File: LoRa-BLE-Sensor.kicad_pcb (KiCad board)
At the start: 4 copper layers, 96 x 60 mm, 129 parts, among them J1 SHF-105-01-X-D-SM, J10 Battery_with_NTC, J11 Conn_01x02_Socket, J12 Conn_01x02_Socket, J2 Conn_01x02_Socket, J3 Battery_with_NTC, J4 Conn_01x06_Socket, J5 Screw_Terminal_01x06, J6 Screw_Terminal_01x06, J7 Screw_Terminal_01x04, J8 Conn_01x04_Pin, J9 Conn_01x04_Pin, Q1 DMN67D7L, Q10 SQ2389ES, Q11 SQ2389ES, Q12 DMN62D0UDW-7, Q13 DMN62D0UDW-7, Q2 DMN67D7L, Q3 DMN67D7L, Q4 DMN67D7L, Q5 DMN67D7L, Q6 DMN67D7L, Q7 DMN67D7L, Q8 DMN67D7L, Q9 SQ2389ES, SW1 SW_Push, SW2 SW_Push, SW3 SW_Push, U1 RAK4630, U2 NPM1300-QEAA-R, U3 TLV61046ADBVR, U4 TLV61046ADBVR, U5 TLV61046ADBVR

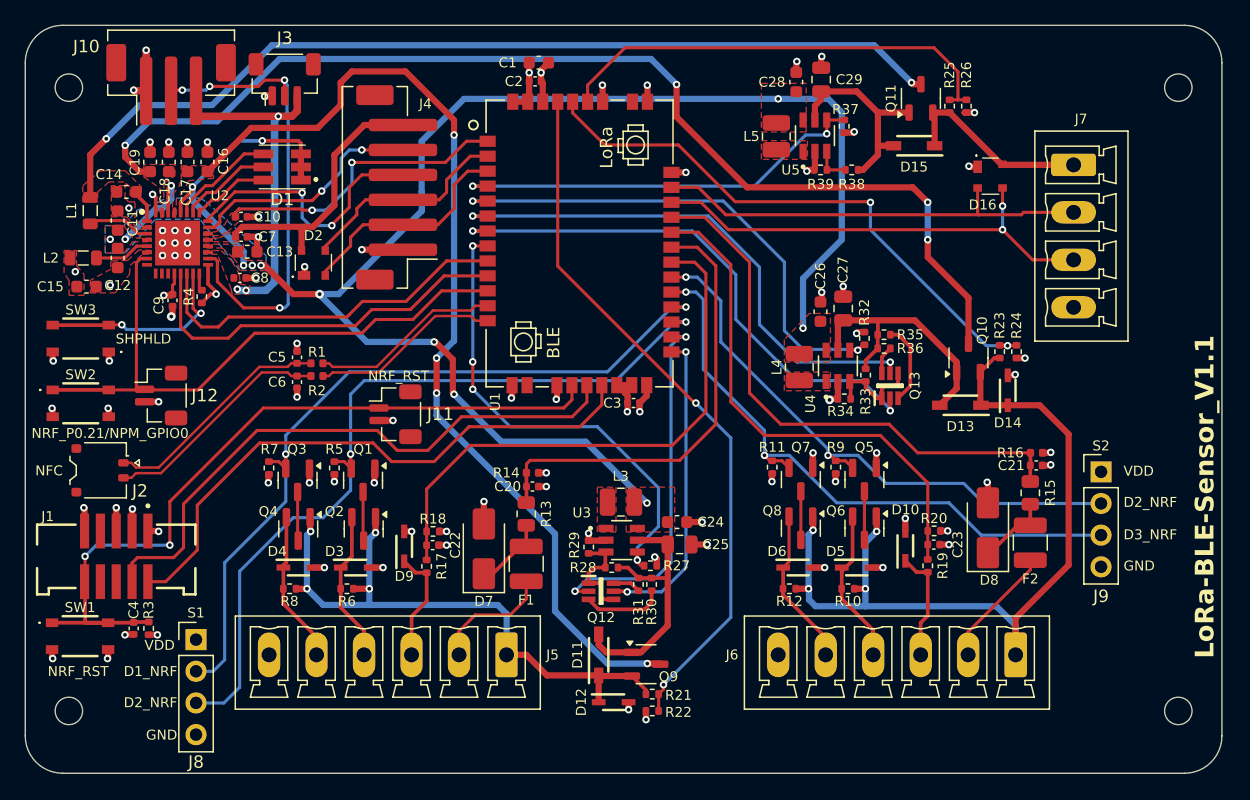
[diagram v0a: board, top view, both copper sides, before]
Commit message: shortened width by 5mm
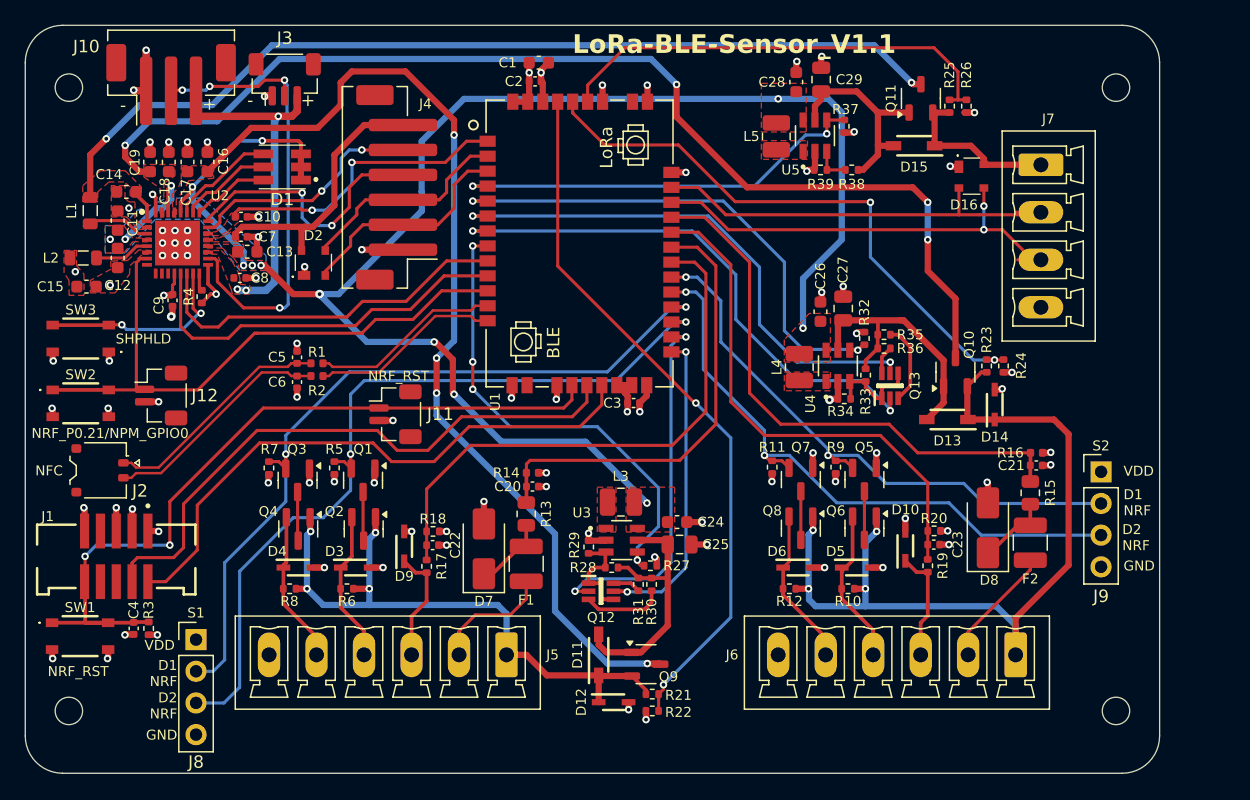
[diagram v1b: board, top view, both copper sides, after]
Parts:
- moved REF** 5.00 mm to (151.5, 54.0)
- moved REF** 5.00 mm to (151.5, 104.0)
- moved J7 2.63 mm to (145.5, 60.2)
- moved D13 1.55 mm to (138.0, 80.6)
- moved R24 1.55 mm to (142.5, 76.3)
- moved D14 1.55 mm to (141.8, 79.4)
- moved Q10 1.55 mm to (138.6, 76.8)
- moved R23 1.55 mm to (141.1, 76.3)
- moved D16 1.50 mm to (139.9, 61.1)
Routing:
- net SENSOR3_PWR: track 15.8 -> 14.7 mm
- net LDO2_OUT: track 89.7 -> 90.4 mm
- net V_SENSOR2_READ: track 46.2 -> 46.9 mm
- net SENSOR2_PWR: track 68.3 -> 68.9 mm
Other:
- board size 96 x 60 mm -> 91 x 60 mm
- board text added: "+"
- board text added: "-"
- board text added: "D1 NRF"
- board text added: "D2 NRF"
- board text removed: "D1_NRF"
- board text removed: "D2_NRF"
- board text removed: "D3_NRF"

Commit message: added docs and manufacturing V1.1
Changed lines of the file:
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@@
 	(paper "A4")
 	(title_block
-		(title "LoRa-BLE-Sensor")
-		(date "2025-03-05")
+		(title "LoRa-BLE-Sensor V1.1")
+		(date "2025-05-28")
 		(rev "1")
-		(company "Cyber Jungle")
+		(company "TerraMatrix")
 	)
 	(layers
@@
 			(drillshape 0)
 			(scaleselection 1)
-			(outputdirectory "Manufacturing/LoRa-BLE-Sensor_V1.0_Gerber/")
+			(outputdirectory "Manufacturing/LoRa-BLE-Sensor_V1.1/LoRa-BLE-Sensor_V1.1_Gerber/")
 		)
 	)
@@
 			(effects
 				(font
-					(size 1 1)
+					(size 0.8 0.8)
 					(thickness 0.15)
 				)
@@
 			(effects
 				(font
-					(size 1 1)
+					(size 0.8 0.8)
 					(thickness 0.15)
 				)
@@
 			(effects
 				(font
-					(size 1 1)
+					(size 0.8 0.8)
 					(thickness 0.15)
 				)
@@
 			(effects
 				(font
-					(size 1 1)
+					(size 0.8 0.8)
 					(thickness 0.15)
 				)
@@
 			(effects
 				(font
-					(size 1 1)
+					(size 0.8 0.8)
 					(thickness 0.15)
 				)
@@
 			(effects
 				(font
-					(size 1 1)
+					(size 0.8 0.8)
 					(thickness 0.15)
 				)
@@
 			(effects
 				(font
-					(size 1 1)
+					(size 0.8 0.8)
 					(thickness 0.15)
 				)
@@
 			(effects
 				(font
-					(size 1 1)
+					(size 0.8 0.8)
 					(thickness 0.15)
 				)
@@
 			(effects
 				(font
-					(size 1 1)
+					(size 0.8 0.8)
 					(thickness 0.15)
 				)
@@
 			(effects
 				(font
-					(size 1 1)
+					(size 0.8 0.8)
 					(thickness 0.15)
 				)
@@
 			(effects
 				(font
-					(size 1 1)
+					(size 0.8 0.8)
 					(thickness 0.15)
 				)
@@
 			(effects
 				(font
-					(size 1 1)
+					(size 0.8 0.8)
 					(thickness 0.15)
 				)
@@
 			(effects
 				(font
-					(size 1 1)
+					(size 0.8 0.8)
 					(thickness 0.15)
 				)
@@
 			(effects
 				(font
-					(size 1 1)
+					(size 0.8 0.8)
 					(thickness 0.15)
 				)
@@
 			(effects
 				(font
-					(size 1 1)
+					(size 0.8 0.8)
 					(thickness 0.15)
 				)
@@
 			(effects
 				(font
-					(size 1 1)
+					(size 0.8 0.8)
 					(thickness 0.15)
 				)
@@
 			(effects
 				(font
-					(size 1 1)
+					(size 0.8 0.8)
 					(thickness 0.15)
 				)
@@
 			(effects
 				(font
-					(size 1 1)
+					(size 0.8 0.8)
 					(thickness 0.15)
 				)
@@
 			(effects
 				(font
-					(size 1 1)
+					(size 0.8 0.8)
 					(thickness 0.15)
 				)
@@
 			(effects
 				(font
-					(size 1.27 1.27)
-					(thickness 0.254)
+					(size 0.8 0.8)
+					(thickness 0.15)
 				)
 			)
@@
 			(effects
 				(font
-					(size 1 1)
+					(size 0.8 0.8)
 					(thickness 0.15)
 				)
@@
 			(effects
 				(font
-					(size 1 1)
+					(size 0.8 0.8)
 					(thickness 0.15)
 				)
@@
 			(effects
 				(font
-					(size 1 1)
+					(size 0.8 0.8)
 					(thickness 0.15)
 				)
@@
 			(effects
 				(font
-					(size 1 1)
+					(size 0.8 0.8)
 					(thickness 0.15)
 				)
@@
 		)
 	)
-	(gr_text_box "Vo2"
+	(gr_text_box "Vo3"
 		(start 149.835 57.48)
 		(end 152.25375 62.09)
@@
 	(segment
 		(start 87.7825 62.2975)
-		(end 89.35 60.73)
+		(end 87.7825 60.4175)
 		(width 0.25)
 		(layer "B.Cu")
@@
 	)
 	(segment
-		(start 89.35 60.73)
-		(end 89.35 59.65)
+		(start 87.7825 60.4175)
+		(end 89.2 59)
 		(width 0.25)
 		(layer "B.Cu")
@@
 	)
 	(segment
-		(start 89.35 59.65)
-		(end 90 59)
-		(width 0.25)
-		(layer "B.Cu")
-		(net 14)
-	)
-	(segment
-		(start 90 59)
+		(start 89.2 59)
 		(end 91 59)
 		(width 0.25)
@@
 	)
 	(segment
-		(start 99.4 58.3)
-		(end 101.094853 58.3)
+		(start 97.7 60)
+		(end 99.4 58.3)
 		(width 0.25)
 		(layer "F.Cu")
@@
 	)
 	(segment
-		(start 97.7 60)
-		(end 99.4 58.3)
+		(start 87.015 63.834669)
+		(end 86.215 63.834669)
+		(width 0.25)
+		(layer "F.Cu")
+		(net 17)
+	)
+	(segment
+		(start 90 60.4)
+		(end 90.4 60)
 		(width 0.25)
 		(layer "F.Cu")
@@
 	)
 	(segment
-		(start 90.2 60)
+		(start 90.4 60)
 		(end 97.7 60)
 		(width 0.25)
@@
 	)
 	(segment
-		(start 87.015 63.834669)
-		(end 86.215 63.834669)
+		(start 99.4 58.3)
+		(end 101.094853 58.3)
 		(width 0.25)
 		(layer "F.Cu")
@@
 	)
 	(via
-		(at 90.2 60)
+		(at 90 60.4)
 		(size 0.6)
 		(drill 0.3)
@@
 	)
 	(segment
-		(start 87.015 63.834669)
-		(end 88.110331 63.834669)
-		(width 0.25)
-		(layer "B.Cu")
-		(net 17)
-	)
-	(segment
-		(start 90.215 61.73)
-		(end 90.215 60.015)
+		(start 88.110331 63.834669)
+		(end 87.015 63.834669)
 		(width 0.25)
 		(layer "B.Cu")
@@
 	)
 	(segment
-		(start 88.110331 63.834669)
-		(end 90.215 61.73)
+		(start 90 60.4)
+		(end 90 61.945)
 		(width 0.25)
 		(layer "B.Cu")
@@
 	)
 	(segment
-		(start 90.215 60.015)
-		(end 90.2 60)
+		(start 90 61.945)
+		(end 88.110331 63.834669)
 		(width 0.25)
 		(layer "B.Cu")

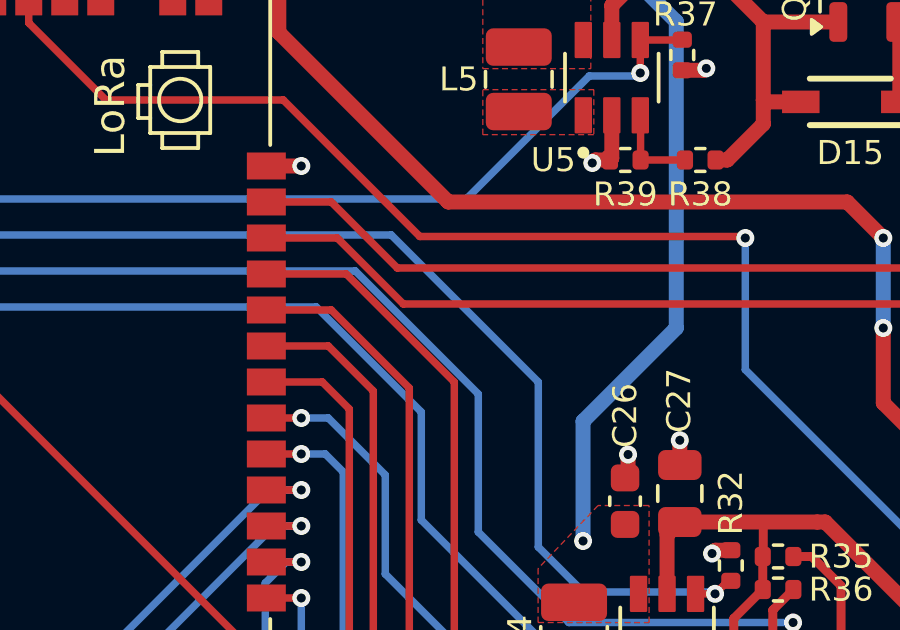
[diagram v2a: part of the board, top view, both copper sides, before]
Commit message: added logo to front
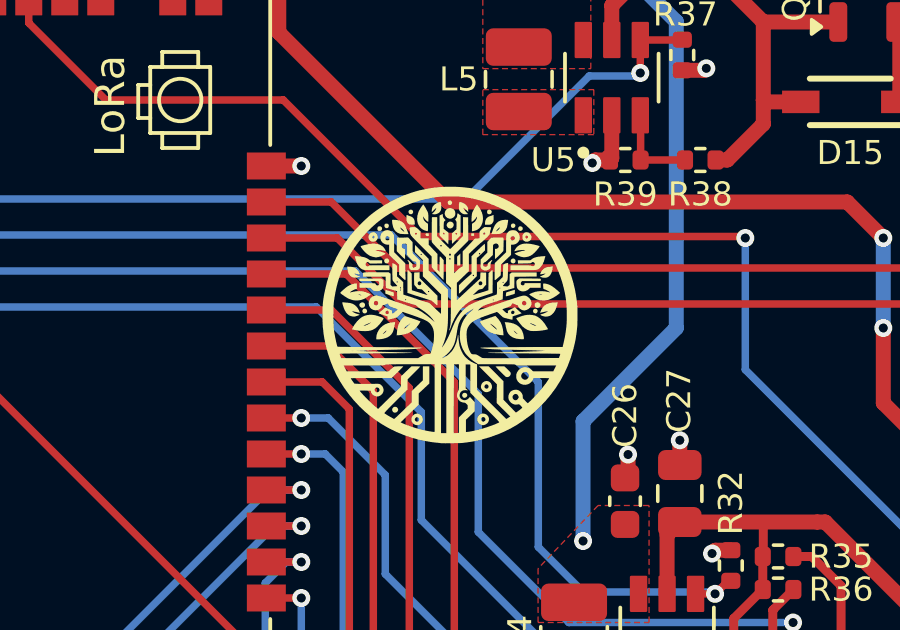
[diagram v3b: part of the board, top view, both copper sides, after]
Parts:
- added G***: LOGO, User_Images:DOE_LOGO_10mm, F.Cu at (122.0, 65.7)
